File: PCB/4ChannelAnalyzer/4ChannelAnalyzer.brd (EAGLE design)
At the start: 91.5 x 91.4 mm, 21 parts, among them U1-ADD-49 ADS1015IDGST, U2-ADD-48 ADS1015IDGST, U3 LM1117MP-3.3, X3 MINI-USB-32005-301

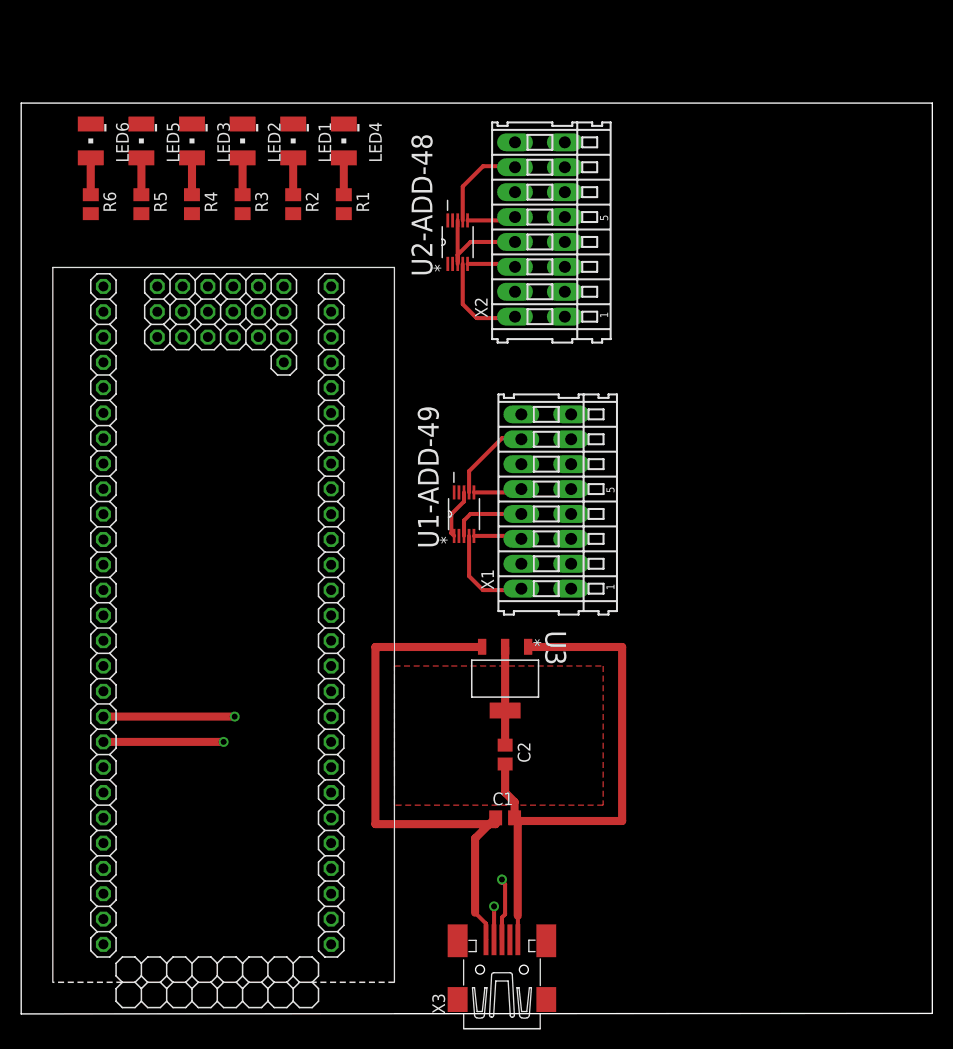
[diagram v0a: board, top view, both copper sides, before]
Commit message: Reorganize board and added Heat sink for voltage stabilizer.
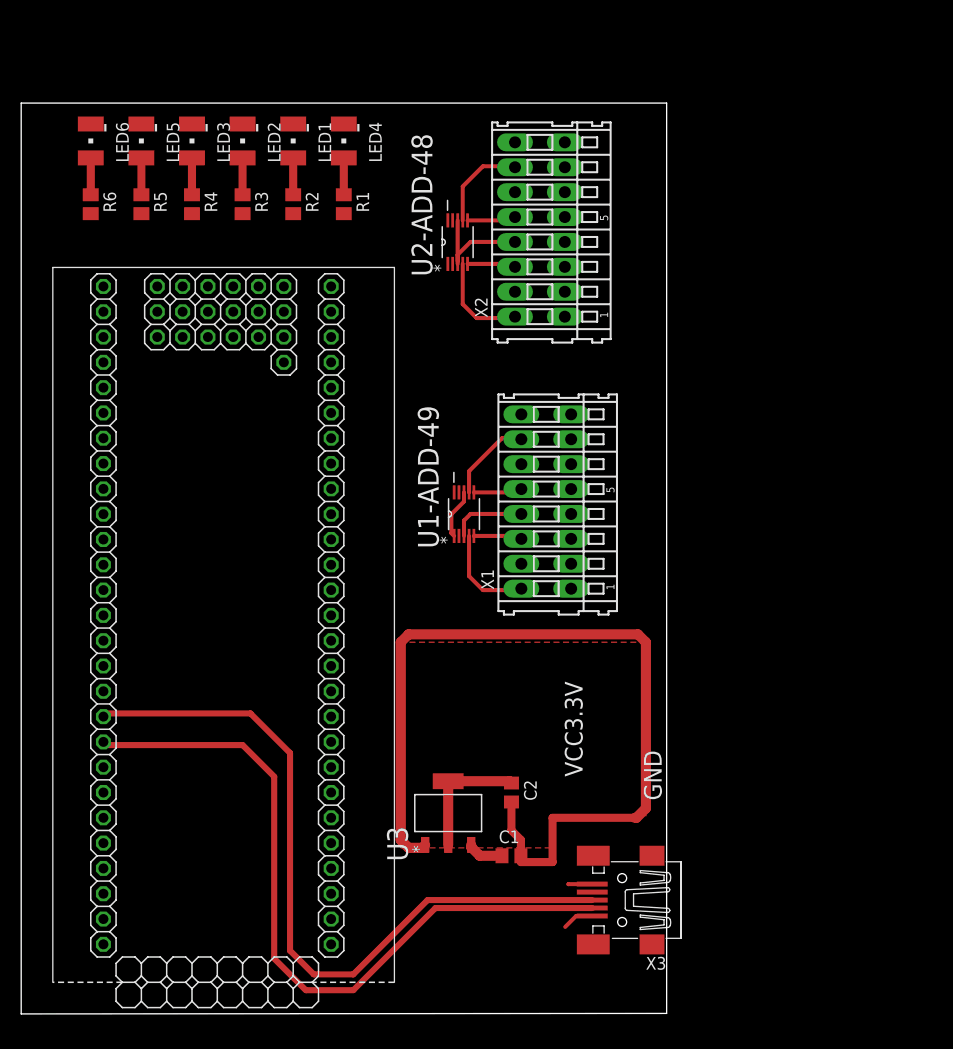
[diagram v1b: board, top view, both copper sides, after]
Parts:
- moved U3 14.7 mm to (42.9, 20.2), turned to 90 degrees
- moved X3 13.9 mm to (60.3, 11.4), turned to 180 degrees
- moved C1 3.86 mm to (49.2, 15.9)
- moved C2 3.86 mm to (49.2, 22.2)
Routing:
- net N$19: track 15.4 -> 73.5 mm, vias 2 -> 0
- net N$20: track 19.5 -> 74.8 mm, vias 2 -> 0
- net USB-5V: track 54.8 -> 6.85 mm
- net GND: track 70.4 -> 105.7 mm
- net VCC3.3V: track 19.0 -> 21.9 mm
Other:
- board size 91.5 x 91.4 mm -> 64.8 x 91.4 mm
- board text added: "GND"
- board text added: "VCC3.3V"

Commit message: Wiring sensors connectors.
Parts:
- moved LED6 86.0 mm to (87.6, 57.8), turned to 90 degrees
- moved LED5 83.2 mm to (87.6, 52.7), turned to 90 degrees
- moved LED3 81.0 mm to (87.6, 47.6), turned to 90 degrees
- moved LED2 79.4 mm to (87.6, 42.5), turned to 90 degrees
- moved LED1 78.5 mm to (87.6, 37.5), turned to 90 degrees
- moved LED4 78.1 mm to (87.6, 32.4), turned to 90 degrees
- moved R6 77.9 mm to (81.3, 57.8), turned to 180 degrees
- moved R5 74.9 mm to (81.3, 52.7), turned to 180 degrees
- moved R4 72.4 mm to (81.3, 47.6), turned to 180 degrees
- moved X2 70.9 mm to (76.2, 12.1), turned to 0 degrees
- moved R3 70.6 mm to (81.3, 42.5), turned to 180 degrees
- moved R2 69.5 mm to (81.3, 37.5), turned to 180 degrees
- moved R1 69.1 mm to (81.3, 32.4), turned to 180 degrees
- moved U2-ADD-48 65.1 mm to (74.9, 20.3), turned to 0 degrees
- moved X3 49.4 mm to (11.4, 4.45), turned to 90 degrees
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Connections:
- net GND: now also LPC1.1
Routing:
- net GND: track 105.7 -> 243.2 mm
- net VCC3.3V: track 21.9 -> 114.8 mm, vias 0 -> 4
- net SCL49: track 0.00 -> 36.8 mm
- net SDA49: track 0.00 -> 36.1 mm
- net USB-5V: track 6.85 -> 20.3 mm, vias 0 -> 2
- net EXT_INT_0: track 0.00 -> 8.29 mm
- net N$19: track 73.5 -> 71.5 mm
- net N$20: track 74.8 -> 73.7 mm
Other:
- board size 64.8 x 91.4 mm -> 91.4 x 64.8 mm
- board text added: "Sensors Connectors"

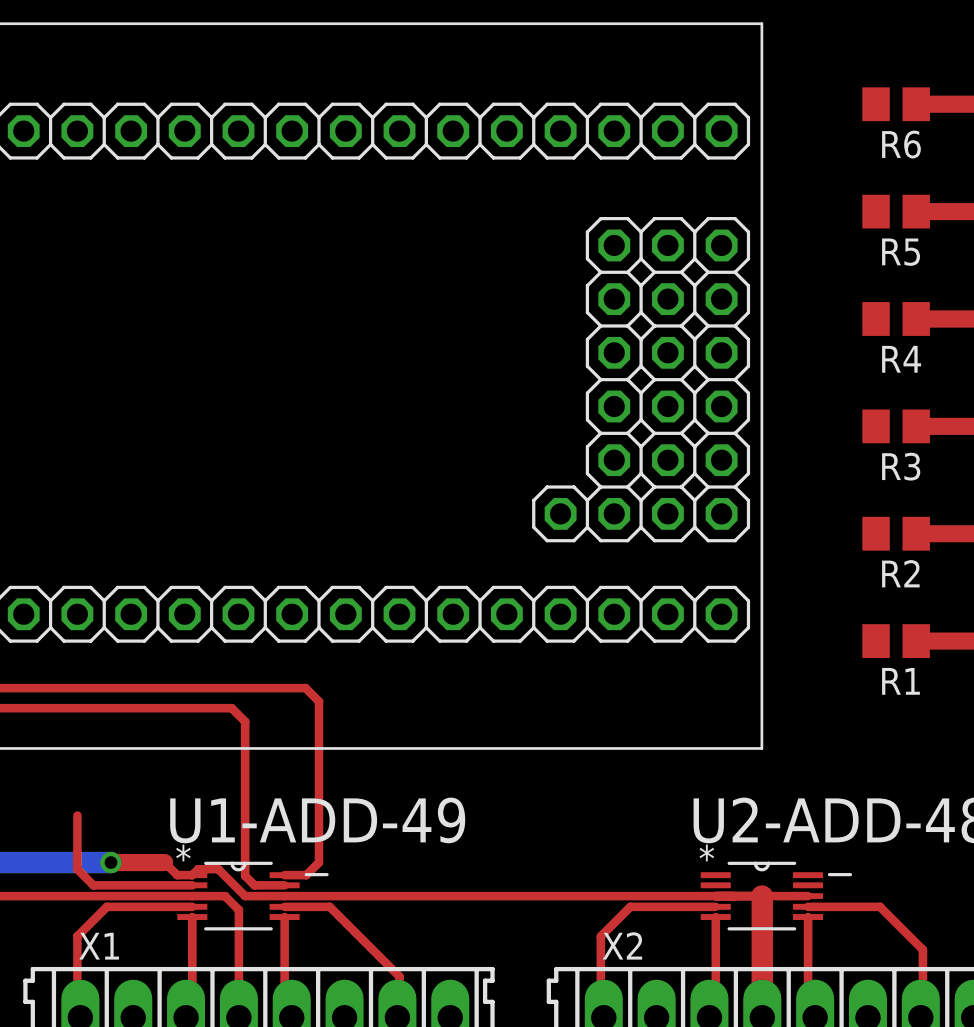
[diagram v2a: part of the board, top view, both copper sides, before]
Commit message: completely wired U2-ADD-48
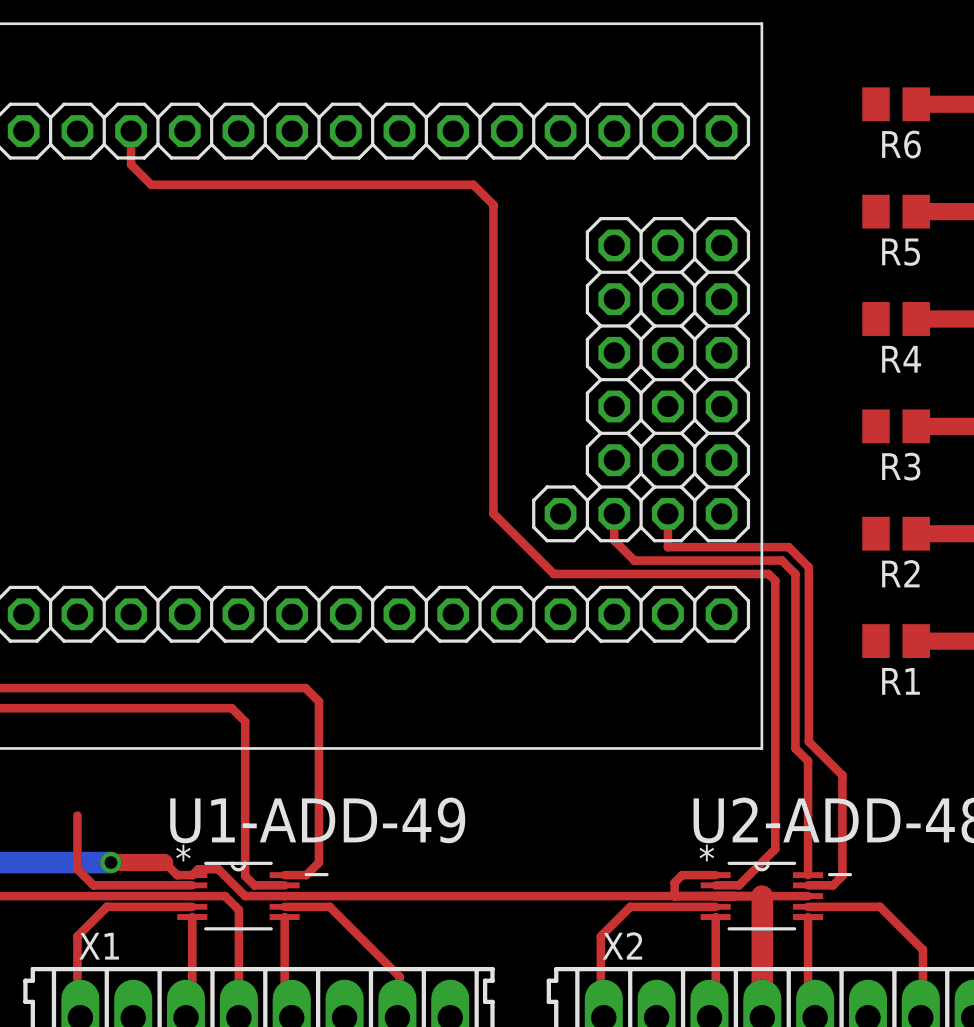
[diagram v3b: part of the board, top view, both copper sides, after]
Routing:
- net EXT_INT_1: track 0.00 -> 65.0 mm
- net SDA48: track 0.00 -> 25.7 mm
- net SCL48: track 0.00 -> 25.0 mm
- net GND: track 243.2 -> 247.9 mm
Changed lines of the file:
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@@
 <wire x1="89.33" y1="37.465" x2="89.33" y2="42.545" width="0" layer="19" extent="1-1"/>
 <wire x1="89.33" y1="32.385" x2="89.33" y2="37.465" width="0" layer="19" extent="1-1"/>
-<wire x1="72.7456" y1="21.3106" x2="72.7456" y2="20.32" width="0" layer="19" extent="1-1"/>
+<wire x1="72.7456" y1="21.3106" x2="71.1581" y2="21.3106" width="0.4064" layer="1"/>
+<wire x1="71.1581" y1="21.3106" x2="70.8025" y2="20.955" width="0.4064" layer="1"/>
+<wire x1="70.8025" y1="20.955" x2="70.8025" y2="20.32" width="0.4064" layer="1"/>
+<wire x1="70.8025" y1="20.32" x2="72.7456" y2="20.32" width="0.4064" layer="1"/>
 </signal>
 <signal name="N$2">
@@
 <contactref element="U2-ADD-48" pad="2"/>
 <contactref element="LPC1" pad="43"/>
-<wire x1="72.7456" y1="20.828" x2="45.085" y2="56.515" width="0" layer="19" extent="1-1"/>
+<wire x1="72.7456" y1="20.828" x2="73.8505" y2="20.828" width="0.4064" layer="1"/>
+<wire x1="73.8505" y1="20.828" x2="75.565" y2="22.5425" width="0.4064" layer="1"/>
+<wire x1="75.565" y1="22.5425" x2="75.565" y2="35.2425" width="0.4064" layer="1"/>
+<wire x1="75.565" y1="35.2425" x2="75.2475" y2="35.56" width="0.4064" layer="1"/>
+<wire x1="75.2475" y1="35.56" x2="65.0875" y2="35.56" width="0.4064" layer="1"/>
+<wire x1="65.0875" y1="35.56" x2="62.23" y2="38.4175" width="0.4064" layer="1"/>
+<wire x1="62.23" y1="38.4175" x2="62.23" y2="53.0225" width="0.4064" layer="1"/>
+<wire x1="62.23" y1="53.0225" x2="61.2775" y2="53.975" width="0.4064" layer="1"/>
+<wire x1="61.2775" y1="53.975" x2="46.0375" y2="53.975" width="0.4064" layer="1"/>
+<wire x1="46.0375" y1="53.975" x2="45.085" y2="54.9275" width="0.4064" layer="1"/>
+<wire x1="45.085" y1="54.9275" x2="45.085" y2="56.515" width="0.4064" layer="1"/>
 </signal>
 <signal name="SCL49">
@@
 <contactref element="U2-ADD-48" pad="10"/>
 <contactref element="LPC1" pad="56"/>
-<wire x1="77.1144" y1="21.3106" x2="67.945" y2="38.4048" width="0" layer="19" extent="1-1"/>
+<wire x1="77.1144" y1="21.3106" x2="77.1144" y2="26.7081" width="0.4064" layer="1"/>
+<wire x1="77.1144" y1="26.7081" x2="76.5175" y2="27.305" width="0.4064" layer="1"/>
+<wire x1="76.5175" y1="27.305" x2="76.5175" y2="35.56" width="0.4064" layer="1"/>
+<wire x1="76.5175" y1="35.56" x2="75.8825" y2="36.195" width="0.4064" layer="1"/>
+<wire x1="75.8825" y1="36.195" x2="68.8975" y2="36.195" width="0.4064" layer="1"/>
+<wire x1="68.8975" y1="36.195" x2="67.945" y2="37.1475" width="0.4064" layer="1"/>
+<wire x1="67.945" y1="37.1475" x2="67.945" y2="38.4048" width="0.4064" layer="1"/>
 </signal>
 <signal name="SDA48">
 <contactref element="U2-ADD-48" pad="9"/>
 <contactref element="LPC1" pad="57"/>
-<wire x1="77.1144" y1="20.828" x2="70.485" y2="38.4048" width="0" layer="19" extent="1-1"/>
+<wire x1="77.1144" y1="20.828" x2="78.2955" y2="20.828" width="0.4064" layer="1"/>
+<wire x1="78.2955" y1="20.828" x2="78.74" y2="21.2725" width="0.4064" layer="1"/>
+<wire x1="78.74" y1="21.2725" x2="78.74" y2="26.035" width="0.4064" layer="1"/>
+<wire x1="78.74" y1="26.035" x2="77.1525" y2="27.6225" width="0.4064" layer="1"/>
+<wire x1="77.1525" y1="27.6225" x2="77.1525" y2="35.8775" width="0.4064" layer="1"/>
+<wire x1="77.1525" y1="35.8775" x2="76.2" y2="36.83" width="0.4064" layer="1"/>
+<wire x1="76.2" y1="36.83" x2="70.485" y2="36.83" width="0.4064" layer="1"/>
+<wire x1="70.485" y1="36.83" x2="70.485" y2="38.4048" width="0.4064" layer="1"/>
 </signal>
 <signal name="N$19">

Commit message: Final design of the of the main module PCB
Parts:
- removed LED1, LED2, LED3, LED4, LED5, LED6: LG_T679-E1F1-1, led:PLCC2
- added J1: (no value), con-amp:10X07MTA
- added R7, R8: 10K, rcl:M0805
- R1, R2, R3, R4, R5, R6: value (none) -> 10
- moved R6 5.75 mm to (80.6, 52.1)
- moved R1 5.43 mm to (80.6, 37.8)
- moved R5 3.55 mm to (80.6, 49.2)
- moved R2 3.24 mm to (80.6, 40.6)
- moved R4 1.42 mm to (80.6, 46.4)
- moved R3 1.14 mm to (80.6, 43.5)
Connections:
- net GND: now also J1.7; no longer LED1.C, LED2.C, LED3.C, LED4.C, LED5.C, LED6.C
- net N$2: now also J1.6; no longer LED4.A
- net N$3: now also J1.5; no longer LED1.A
- net N$4: now also J1.4; no longer LED2.A
- net N$5: now also J1.3; no longer LED3.A
- net N$6: now also J1.2; no longer LED5.A
- net N$7: now also J1.1; no longer LED6.A
- net SCL49: now also R8.1
- net SDA49: now also R7.1
- net VCC3.3V: now also R7.2, R8.2
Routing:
- net EXT_INT_0: track 8.29 -> 41.0 mm, vias 0 -> 2
- net N$26: track 0.00 -> 7.07 mm
- net N$25: track 0.00 -> 6.94 mm
- net N$21: track 0.00 -> 6.93 mm
- net N$24: track 0.00 -> 6.81 mm
- net N$22: track 0.00 -> 6.80 mm
- net N$23: track 0.00 -> 6.68 mm
- net VCC3.3V: track 114.8 -> 119.6 mm
- net GND: track 247.9 -> 250.1 mm
- net SDA49: track 36.1 -> 38.3 mm
- net SCL49: track 36.8 -> 38.4 mm
- net N$7: track 3.70 -> 5.16 mm
- net N$6: track 3.70 -> 5.03 mm
- net N$2: track 3.70 -> 5.03 mm
- net N$3: track 3.70 -> 4.90 mm
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- added copper zone on layer 1, net GND

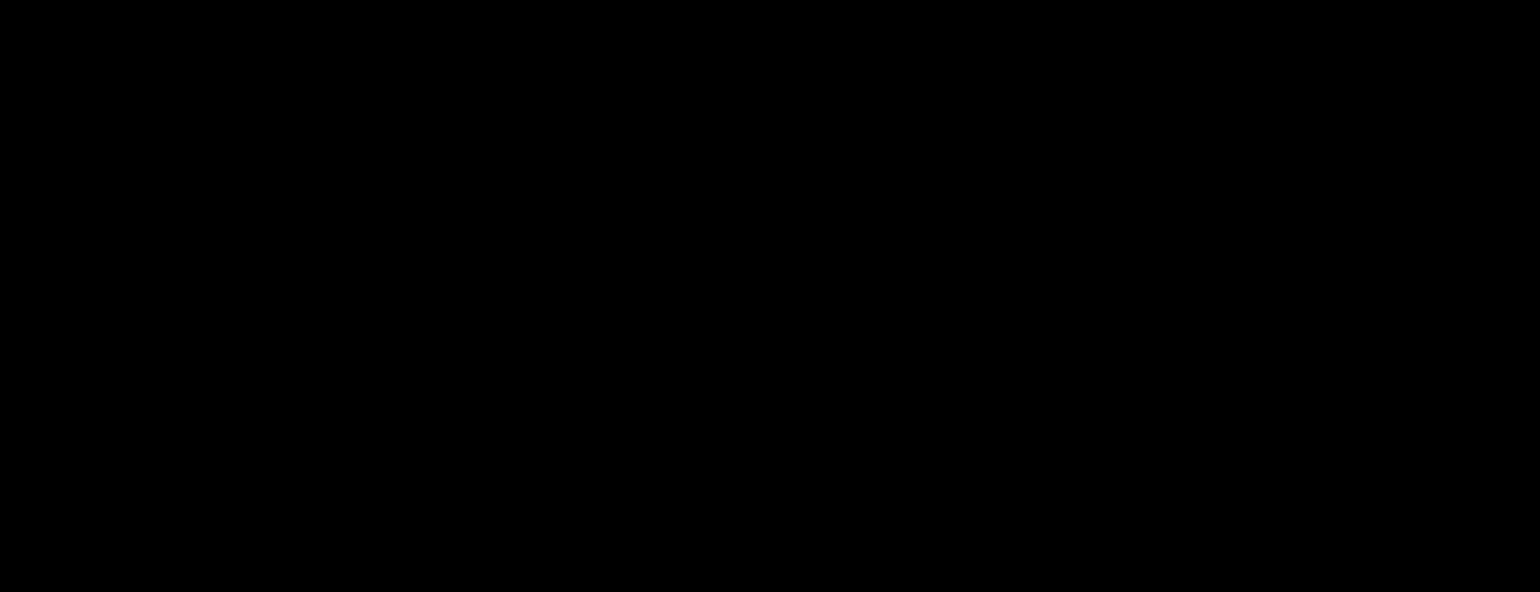
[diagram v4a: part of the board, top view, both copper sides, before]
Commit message: Added ACR1000 in to circuit and PCB design
Creating New Sheet for sensors module.
Added ARC1000 in to design.
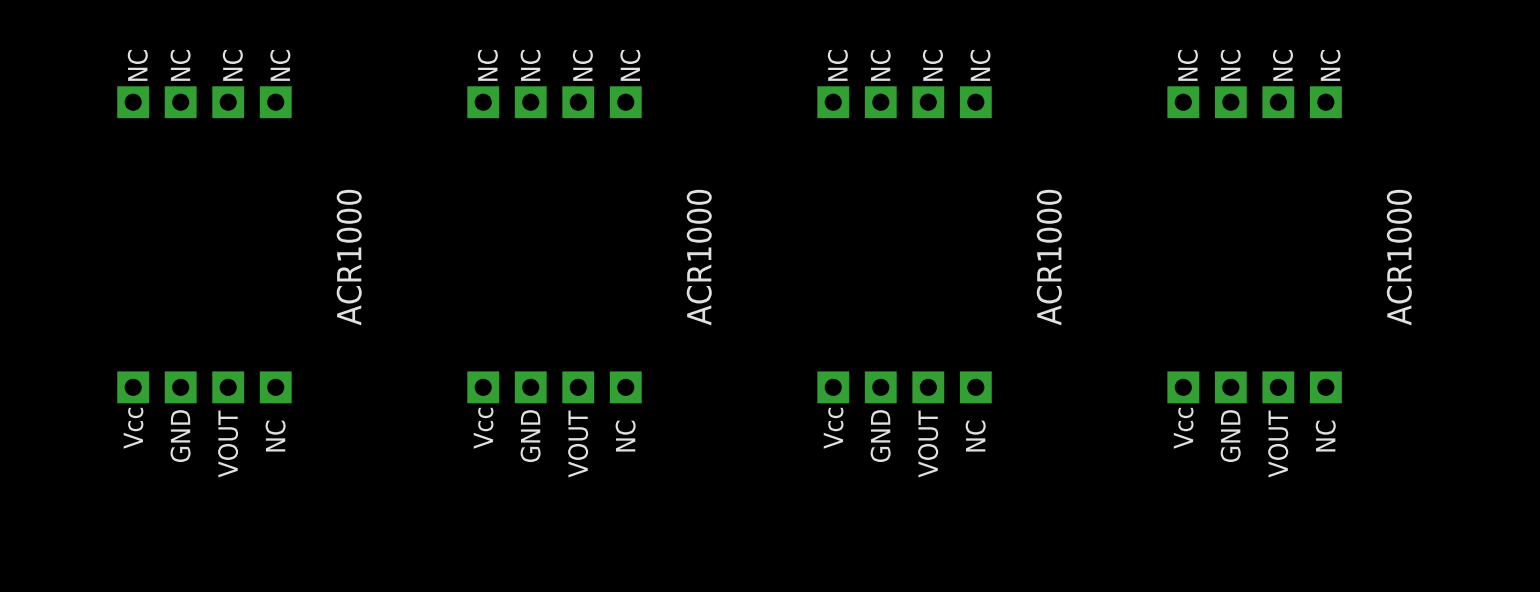
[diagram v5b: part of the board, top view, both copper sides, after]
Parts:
- added U$1, U$2, U$3, U$4: ACR1000, ACR1000:ACR1000
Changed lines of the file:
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@@
 <setting verticaltext="up"/>
 </settings>
-<grid distance="0.0125" unitdist="inch" unit="inch" style="lines" multiple="1" display="yes" altdistance="0.025" altunitdist="inch" altunit="inch"/>
+<grid distance="0.025" unitdist="inch" unit="inch" style="lines" multiple="1" display="yes" altdistance="0.025" altunitdist="inch" altunit="inch"/>
 <layers>
 <layer number="1" name="Top" color="4" fill="1" visible="yes" active="yes"/>
@@
 <element name="R8" library="rcl" package="M0805" value="10K" x="56.515" y="21.9075"/>
 <element name="J1" library="con-amp" package="10X07MTA" value="" x="86.36" y="43.4975" rot="R90"/>
+<element name="U$1" library="ACR1000" package="ACR1000" value="ACR1000" x="19.685" y="88.9" rot="R90"/>
+<element name="U$2" library="ACR1000" package="ACR1000" value="ACR1000" x="38.1" y="88.9" rot="R90"/>
+<element name="U$3" library="ACR1000" package="ACR1000" value="ACR1000" x="56.515" y="88.9" rot="R90"/>
+<element name="U$4" library="ACR1000" package="ACR1000" value="ACR1000" x="74.93" y="88.9" rot="R90"/>
 </elements>
 <signals>
